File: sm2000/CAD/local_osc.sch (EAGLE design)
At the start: 16 parts, among them U1 SI5351A, U2 SI570CAC000141DG

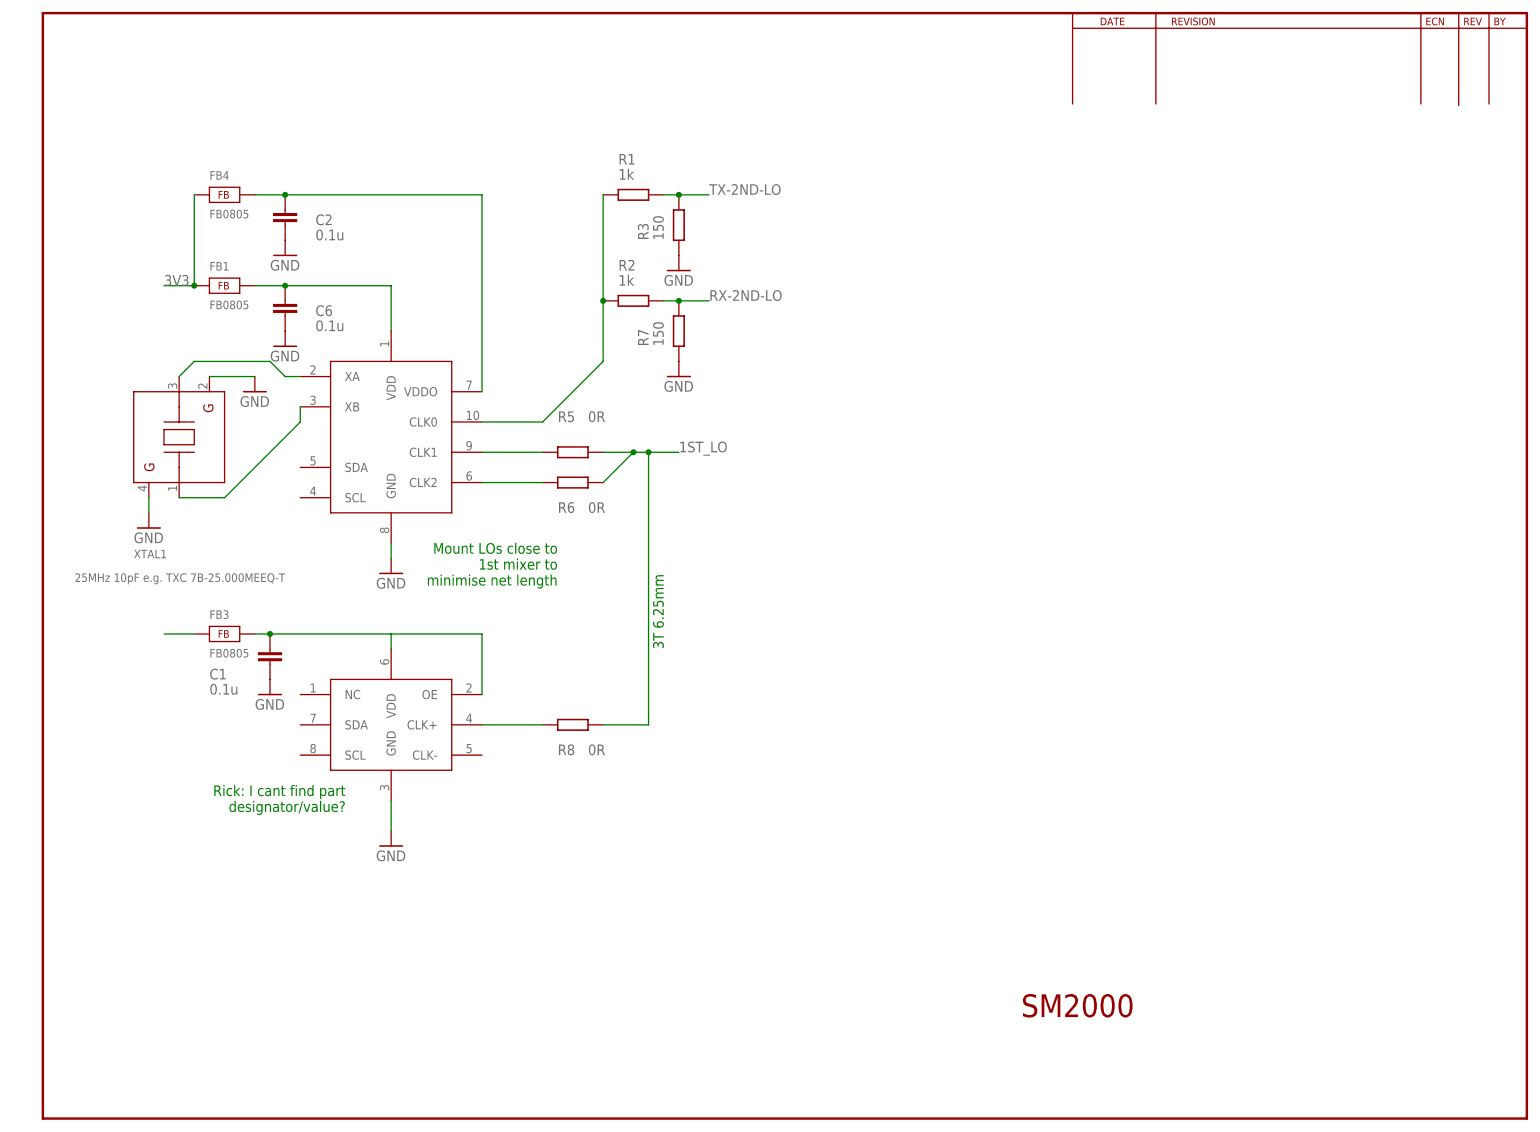
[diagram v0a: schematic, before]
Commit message: aDDED lOCAL oSCILLATOR CIRCUITRY TO sm2000 sch. MOVED 3.3V PS TO SHT 4. CONTINUED SCHEMATIC CLEANUP RGB
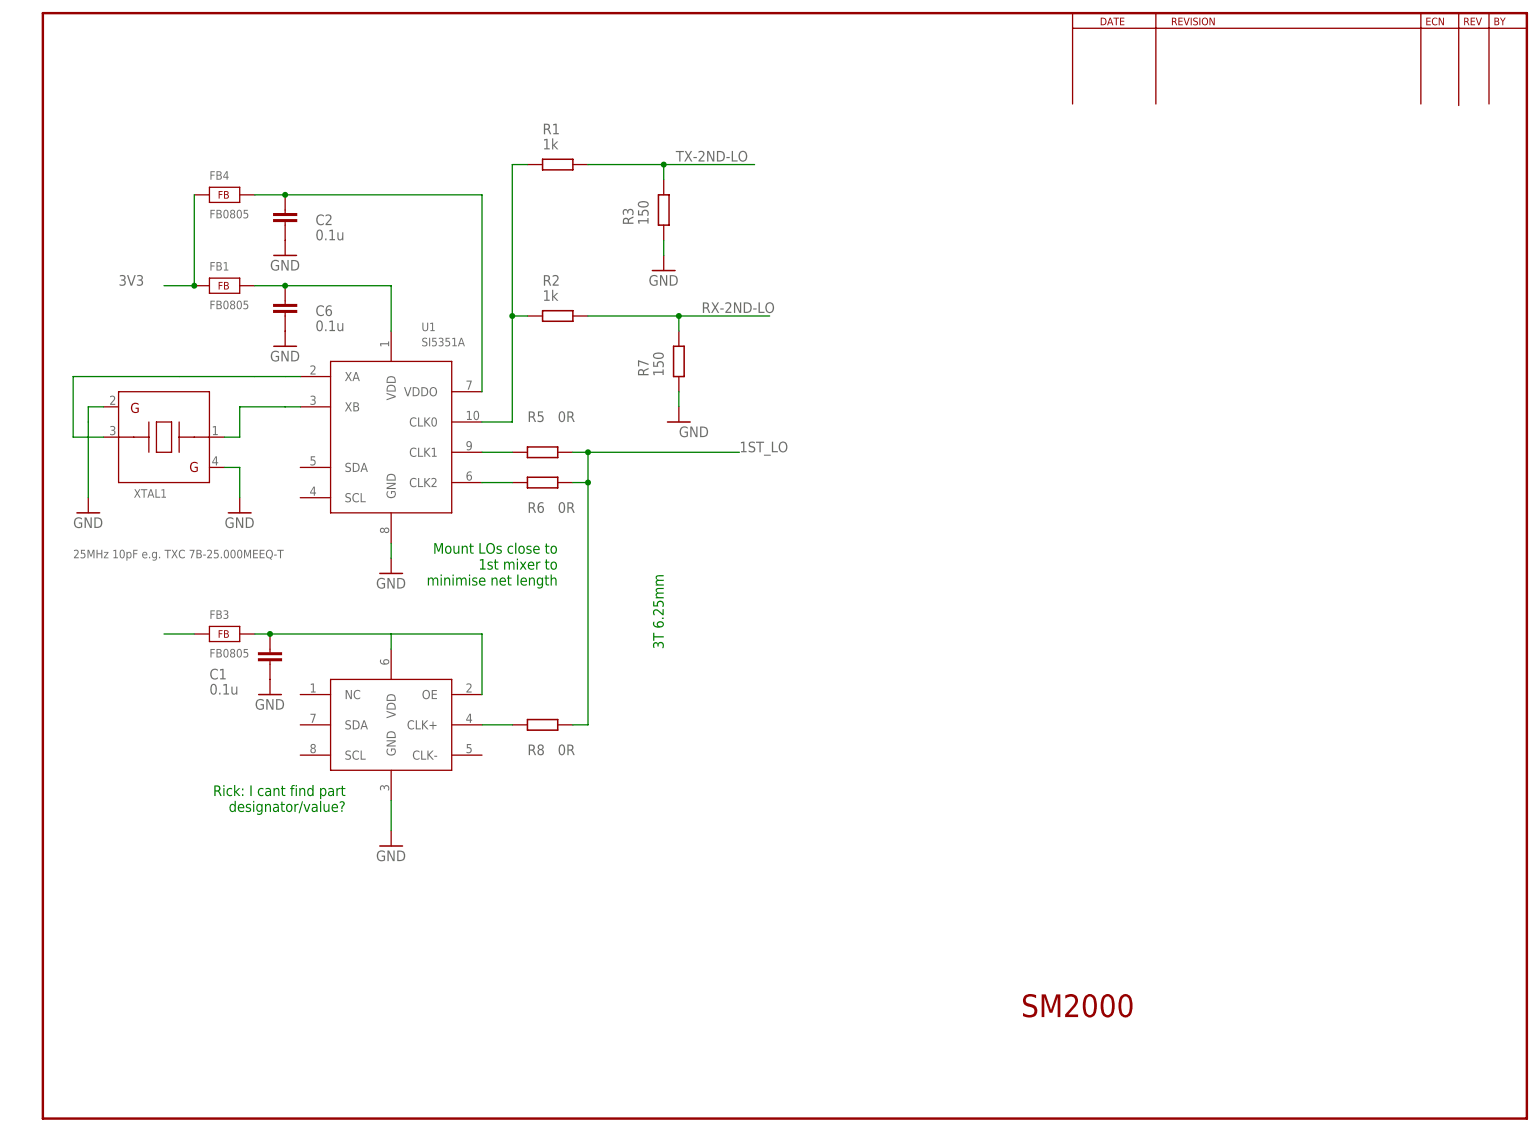
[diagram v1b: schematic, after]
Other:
- moved on the sheet: R1, R2, R3, R5, R6, R7, R8, XTAL1

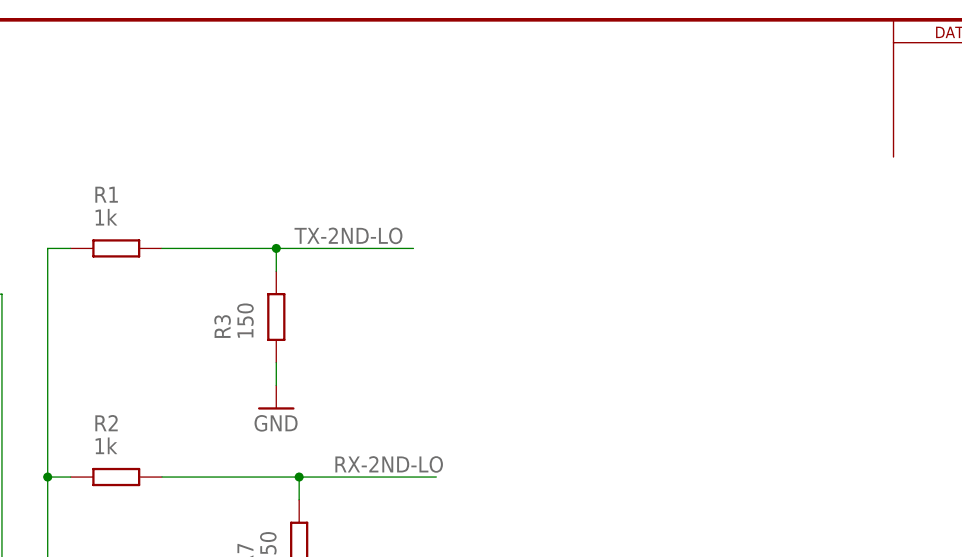
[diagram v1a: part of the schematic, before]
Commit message: added diode switch to TX 2nd lo and pwr sensor
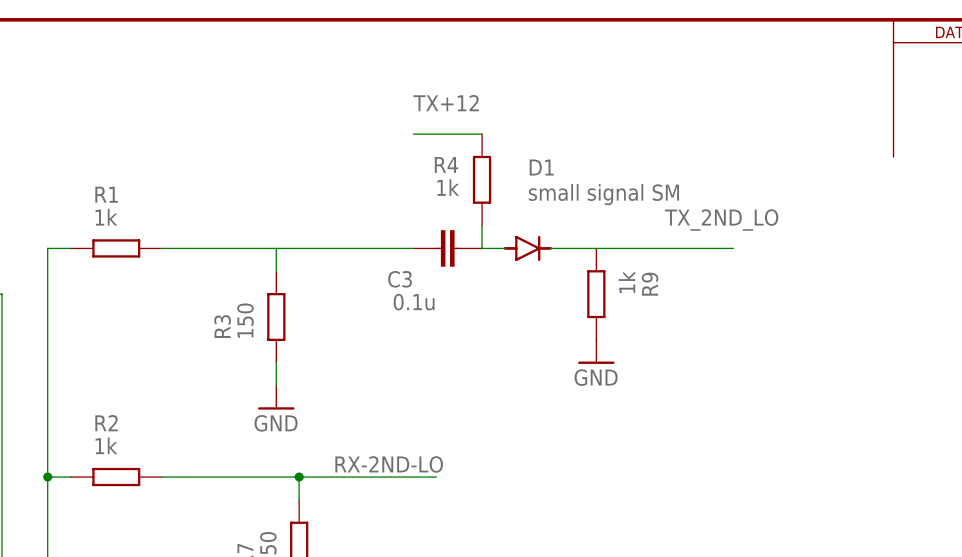
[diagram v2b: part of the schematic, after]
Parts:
- added C3: 0.1u, rcl:C-EU025-024X044
- added D1: small signal SM, _RoweTel:DIODE-DO-214AC
- added R4, R9: 1k, AA-ipc-7351-resistor:RESISTOR_0805
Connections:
- removed net TX-2ND-LO: R1.1, R3.1
- new net N$12: C3.2, D1.A, R4.2
- new net N$7: C3.1, R1.1, R3.1
- new net TX+12: R4.1
- new net TX_2ND_LO: D1.C
- net GND: now also R9.1
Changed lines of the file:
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@@
 <?xml version="1.0" encoding="utf-8"?>
 <!DOCTYPE eagle SYSTEM "eagle.dtd">
-<eagle version="6.5.0">
+<eagle version="7.2.0">
 <drawing>
 <settings>
@@
 <setting verticaltext="up"/>
 </settings>
-<grid distance="0.1" unitdist="inch" unit="inch" style="lines" multiple="1" display="yes" altdistance="0.01" altunitdist="inch" altunit="inch"/>
+<grid distance="0.1" unitdist="inch" unit="inch" style="lines" multiple="1" display="no" altdistance="0.01" altunitdist="inch" altunit="inch"/>
 <layers>
 <layer number="1" name="Top" color="4" fill="1" visible="no" active="no"/>
@@
 <part name="R8" library="AA-ipc-7351-resistor" deviceset="RESISTOR_" device="0805" value="0R"/>
 <part name="U1" library="_RoweTel" deviceset="SI5351A" device=""/>
+<part name="R4" library="AA-ipc-7351-resistor" deviceset="RESISTOR_" device="0805" value="1k"/>
+<part name="C3" library="rcl" deviceset="C-EU" device="025-024X044" value="0.1u"/>
+<part name="R9" library="AA-ipc-7351-resistor" deviceset="RESISTOR_" device="0805" value="1k"/>
+<part name="D1" library="_RoweTel" deviceset="DIODE-" device="DO-214AC" value="small signal SM"/>
+<part name="GND10" library="supply1" deviceset="GND" device=""/>
 </parts>
 <sheets>
@@
 </instance>
 <instance part="U1" gate="G$1" x="58.42" y="114.3"/>
+<instance part="R4" gate="G$1" x="127" y="167.64" smashed="yes" rot="R270">
+<attribute name="NAME" x="124.46" y="170.18" size="1.778" layer="95" rot="R180"/>
+<attribute name="VALUE" x="124.46" y="167.64" size="1.778" layer="96" rot="R180"/>
+</instance>
+<instance part="C3" gate="G$1" x="121.92" y="160.02" smashed="yes" rot="R90">
+<attribute name="NAME" x="119.38" y="157.48" size="1.778" layer="95" rot="R180"/>
+<attribute name="VALUE" x="121.92" y="154.94" size="1.778" layer="96" rot="R180"/>
+</instance>
+<instance part="R9" gate="G$1" x="139.7" y="154.94" smashed="yes" rot="R90">
+<attribute name="NAME" x="144.78" y="157.48" size="1.778" layer="95" rot="R270"/>
+<attribute name="VALUE" x="142.24" y="157.48" size="1.778" layer="96" rot="R270"/>
+</instance>
+<instance part="D1" gate="G$1" x="132.08" y="160.02" smashed="yes">
+<attribute name="NAME" x="132.08" y="168.1226" size="1.778" layer="95"/>
+<attribute name="VALUE" x="132.08" y="165.3286" size="1.778" layer="96"/>
+</instance>
+<instance part="GND10" gate="1" x="139.7" y="147.32" smashed="yes">
+<attribute name="VALUE" x="137.16" y="144.78" size="1.778" layer="96"/>
+</instance>
 </instances>
 <busses>
@@
 <pinref part="R7" gate="G$1" pin="2"/>
 <wire x1="106.68" y1="119.38" x2="106.68" y2="121.92" width="0.1524" layer="91"/>
+</segment>
+<segment>
+<pinref part="R9" gate="G$1" pin="1"/>
+<pinref part="GND10" gate="1" pin="GND"/>
 </segment>
 </net>
@@
 <wire x1="73.66" y1="71.12" x2="73.66" y2="81.28" width="0.1524" layer="91"/>
 <wire x1="73.66" y1="81.28" x2="58.42" y2="81.28" width="0.1524" layer="91"/>
-</segment>
-</net>
-<net name="TX-2ND-LO" class="0">
-<segment>
-<pinref part="R3" gate="G$1" pin="1"/>
-<wire x1="104.14" y1="157.48" x2="104.14" y2="160.02" width="0.1524" layer="91"/>
-<wire x1="104.14" y1="160.02" x2="119.38" y2="160.02" width="0.1524" layer="91"/>
-<label x="106.172" y="160.528" size="1.778" layer="95"/>
-<pinref part="R1" gate="G$1" pin="1"/>
-<wire x1="104.14" y1="160.02" x2="91.44" y2="160.02" width="0.1524" layer="91"/>
-<junction x="104.14" y="160.02"/>
 </segment>
 </net>
@@
 </segment>
 </net>
+<net name="N$7" class="0">
+<segment>
+<pinref part="R1" gate="G$1" pin="1"/>
+<pinref part="C3" gate="G$1" pin="1"/>
+<wire x1="91.44" y1="160.02" x2="104.14" y2="160.02" width="0.1524" layer="91"/>
+<pinref part="R3" gate="G$1" pin="1"/>
+<wire x1="104.14" y1="160.02" x2="119.38" y2="160.02" width="0.1524" layer="91"/>
+<wire x1="104.14" y1="157.48" x2="104.14" y2="160.02" width="0.1524" layer="91"/>
+</segment>
+</net>
+<net name="N$12" class="0">
+<segment>
+<pinref part="C3" gate="G$1" pin="2"/>
+<pinref part="D1" gate="G$1" pin="A"/>
+<wire x1="127" y1="160.02" x2="129.54" y2="160.02" width="0.1524" layer="91"/>
+<pinref part="R4" gate="G$1" pin="2"/>
+<wire x1="127" y1="162.56" x2="127" y2="160.02" width="0.1524" layer="91"/>
+</segment>
+</net>
+<net name="TX_2ND_LO" class="0">
+<segment>
+<pinref part="D1" gate="G$1" pin="C"/>
+<wire x1="134.62" y1="160.02" x2="154.94" y2="160.02" width="0.1524" layer="91"/>
+<label x="147.32" y="162.56" size="1.778" layer="95"/>
+</segment>
+</net>
+<net name="TX+12" class="0">
+<segment>
+<pinref part="R4" gate="G$1" pin="1"/>
+<wire x1="127" y1="172.72" x2="119.38" y2="172.72" width="0.1524" layer="91"/>
+<label x="119.38" y="175.26" size="1.778" layer="95"/>
+</segment>
+</net>
